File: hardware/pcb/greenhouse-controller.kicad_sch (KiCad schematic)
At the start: 47 parts, among them J1 Motor 2, J2 Screw_Terminal_01x02, J3 I2C Display, J4 Keypad, J5 MODBUS RS485, J6 Motor 3, J7 Motor 1, Q1 2N7000, Q2 2N7000, Q3 2N7000, Q4 2N7000, Q5 2N7000, Q6 2N7000, U1 Wemos_S3_ESP32-S3, U2 BUCK-30V-5V

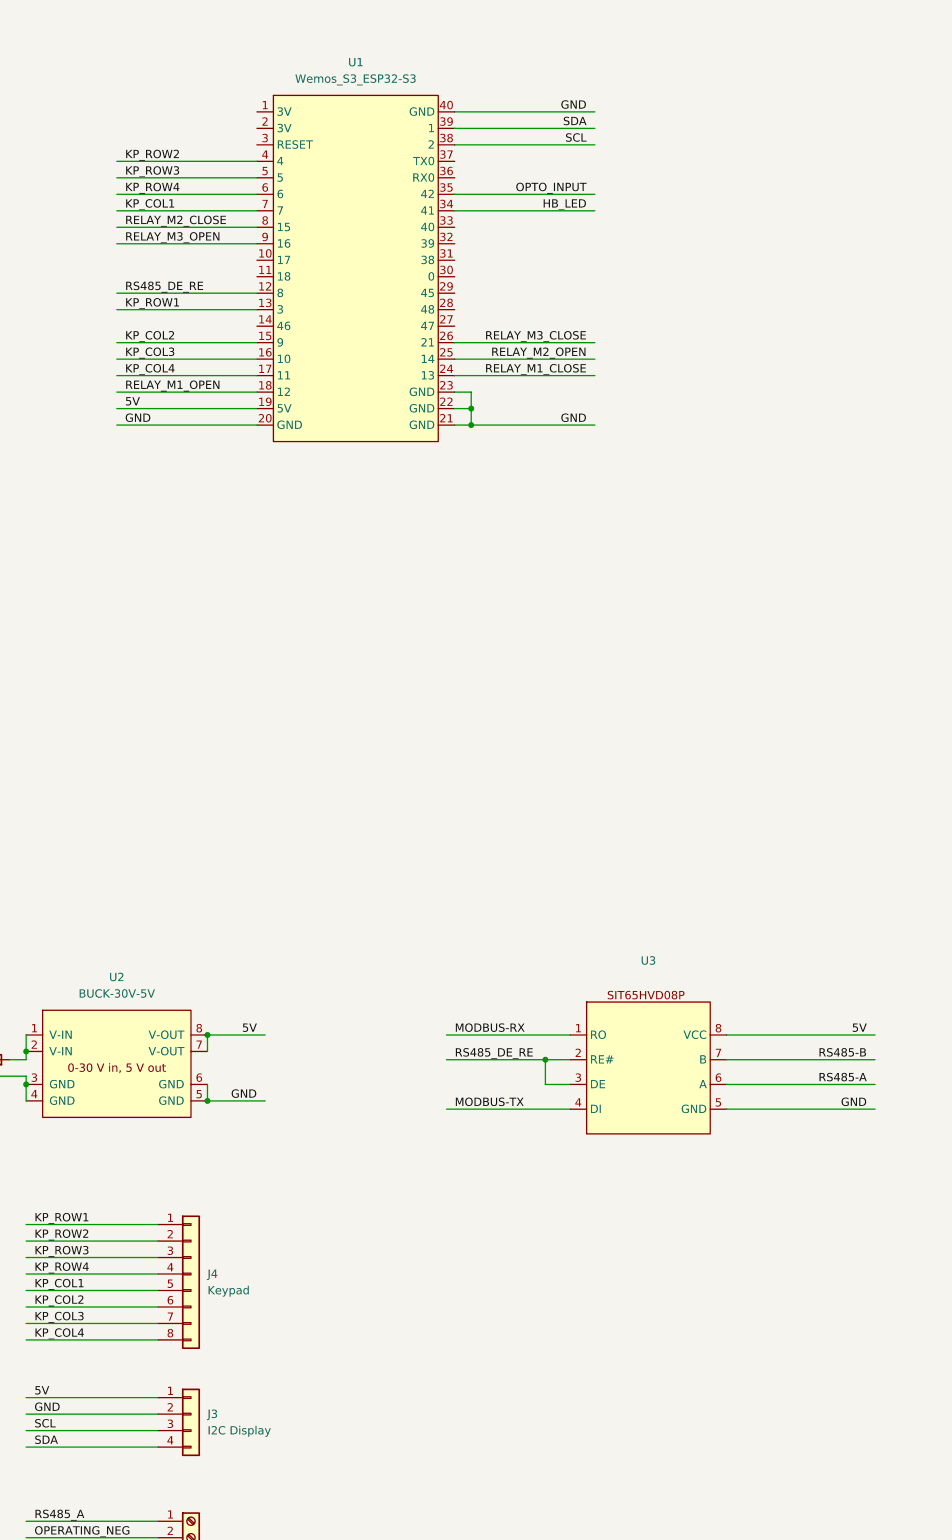
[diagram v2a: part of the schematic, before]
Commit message: Added Atomic RS485 Base documentation for development of stubs and tests. added LittleFS driver added modbus drive (not ready) added nvs driver added sdcard driver Updated PCD design
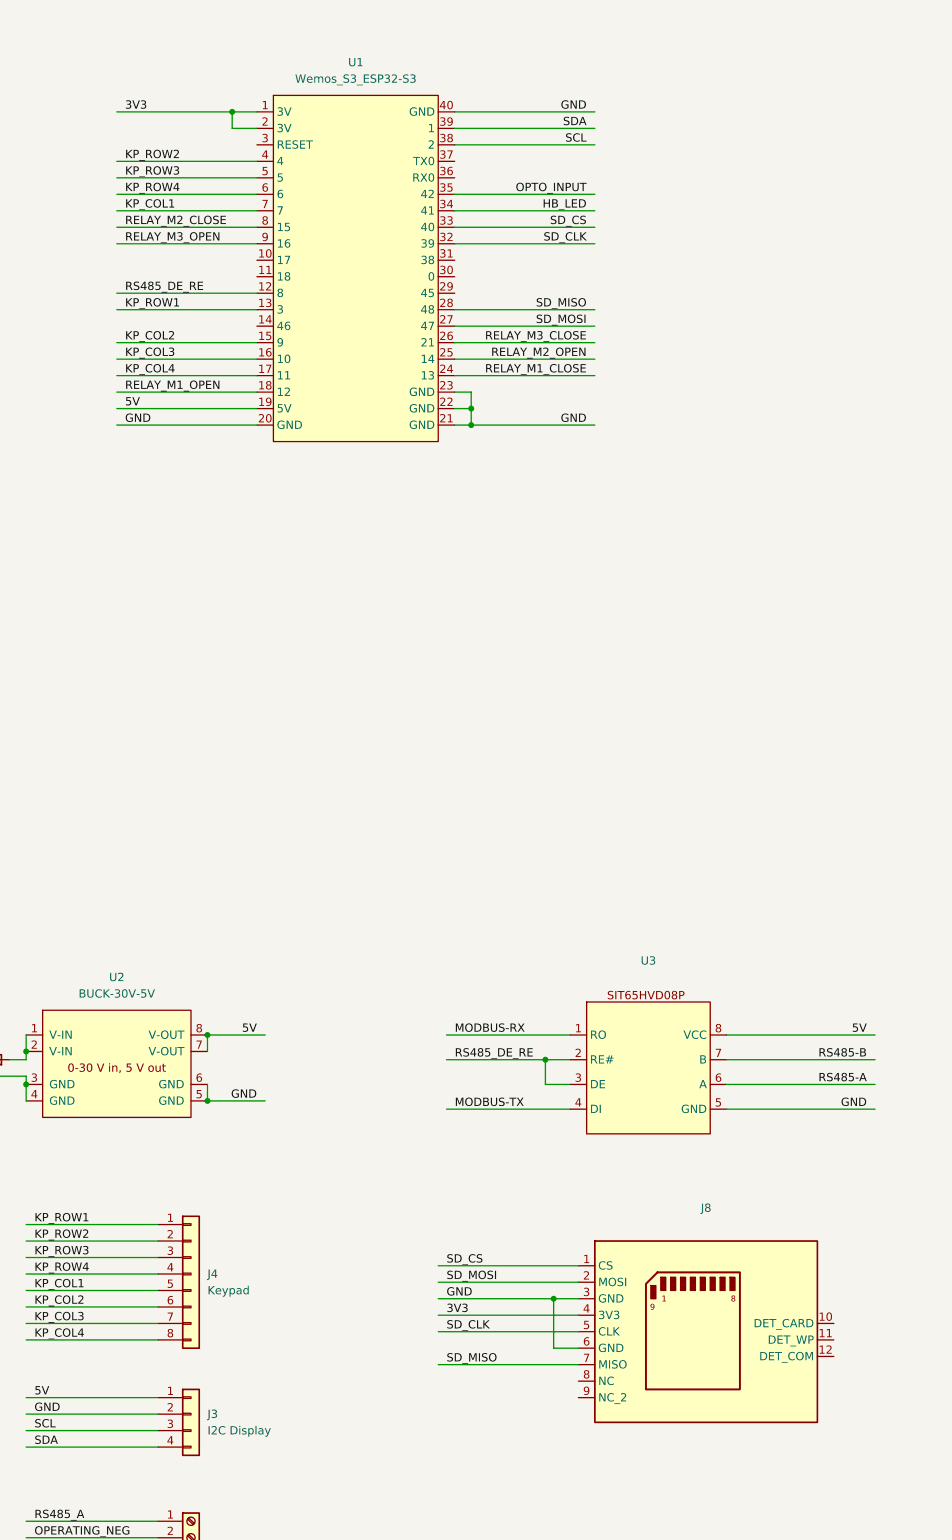
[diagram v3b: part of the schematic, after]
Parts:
- added J8: ~, symbol my-KiCad-library:SD-Socket
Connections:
- net GND: now also J8.3 (GND), J8.6 (GND)
- net 3V3: now reaches U1.1 (3V)
- net 3V3: now also U1.2 (3V), J8.4 (3V3)
- net SD_MOSI: now reaches U1.27 (47)
- net SD_MOSI: now also J8.2 (MOSI)
- net SD_MISO: now reaches U1.28 (48)
- net SD_MISO: now also J8.7 (MISO)
- net SD_CLK: now reaches U1.32 (39)
- net SD_CLK: now also J8.5 (CLK)
- net SD_CS: now reaches U1.33 (40)
- net SD_CS: now also J8.1 (CS)

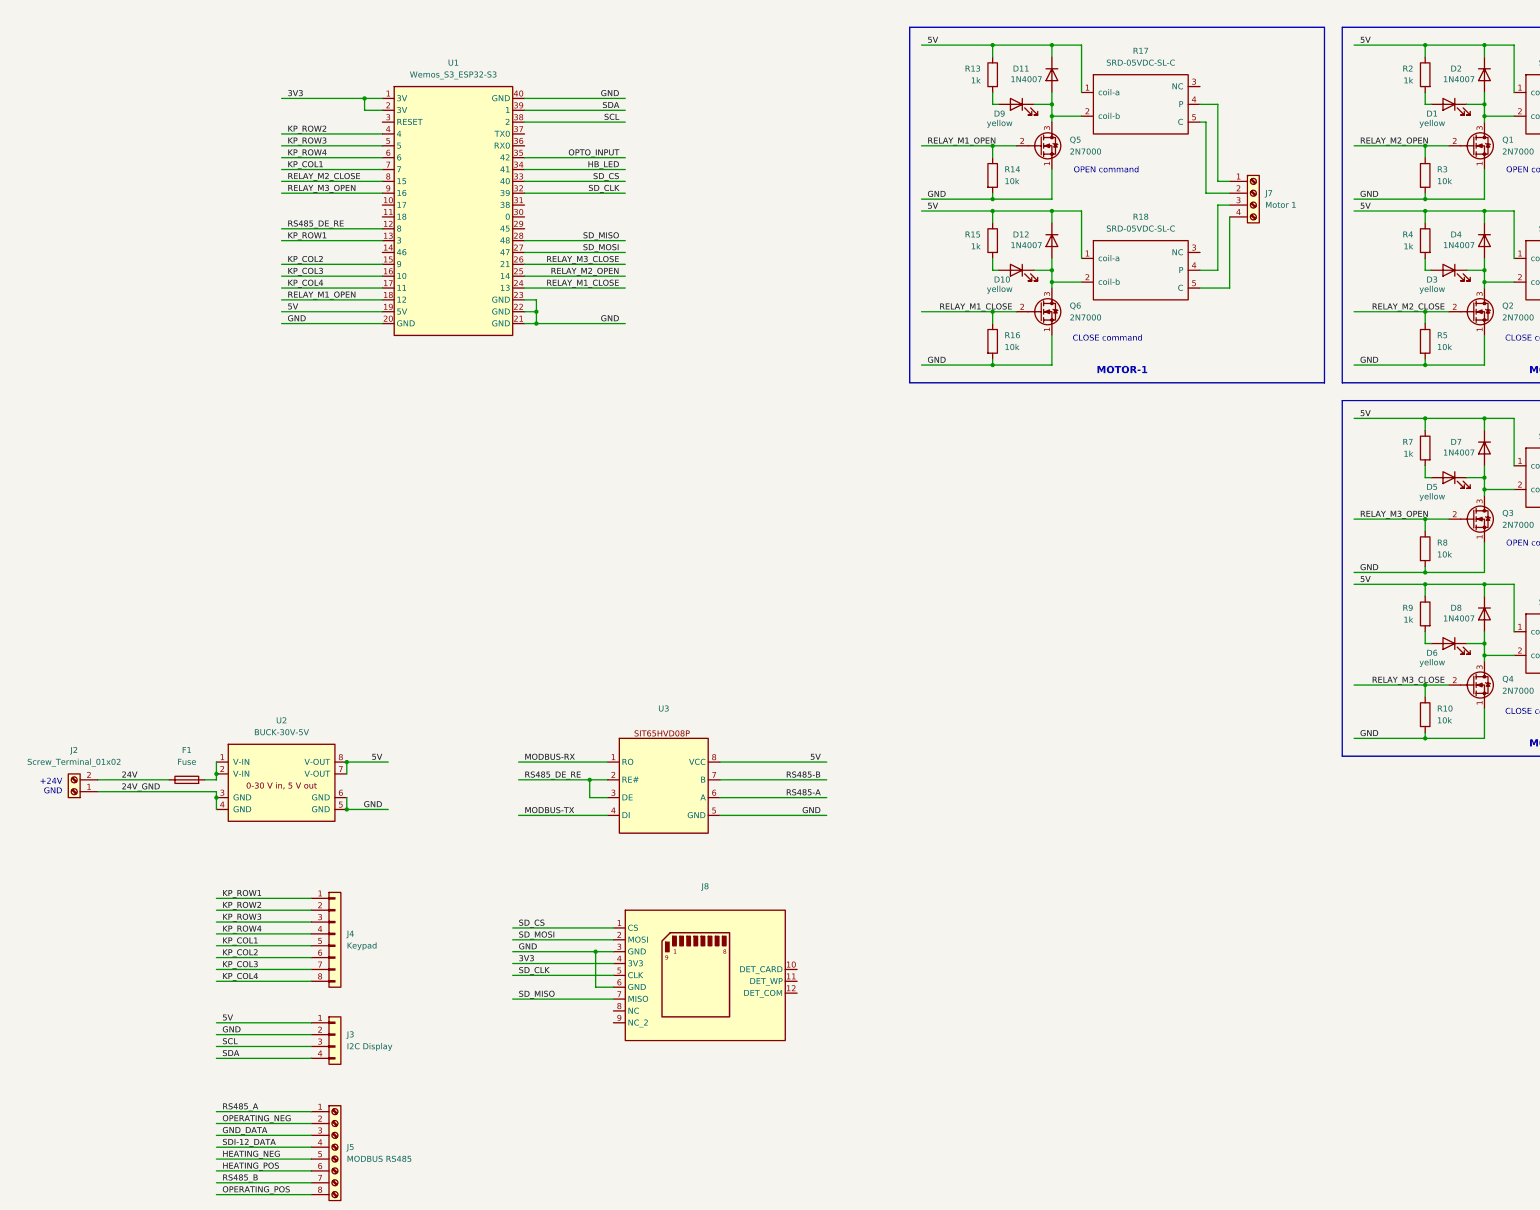
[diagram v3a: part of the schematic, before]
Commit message: updated design documentation with changes during implementation. added functional design items on led-colour use. updated schema in Kicad
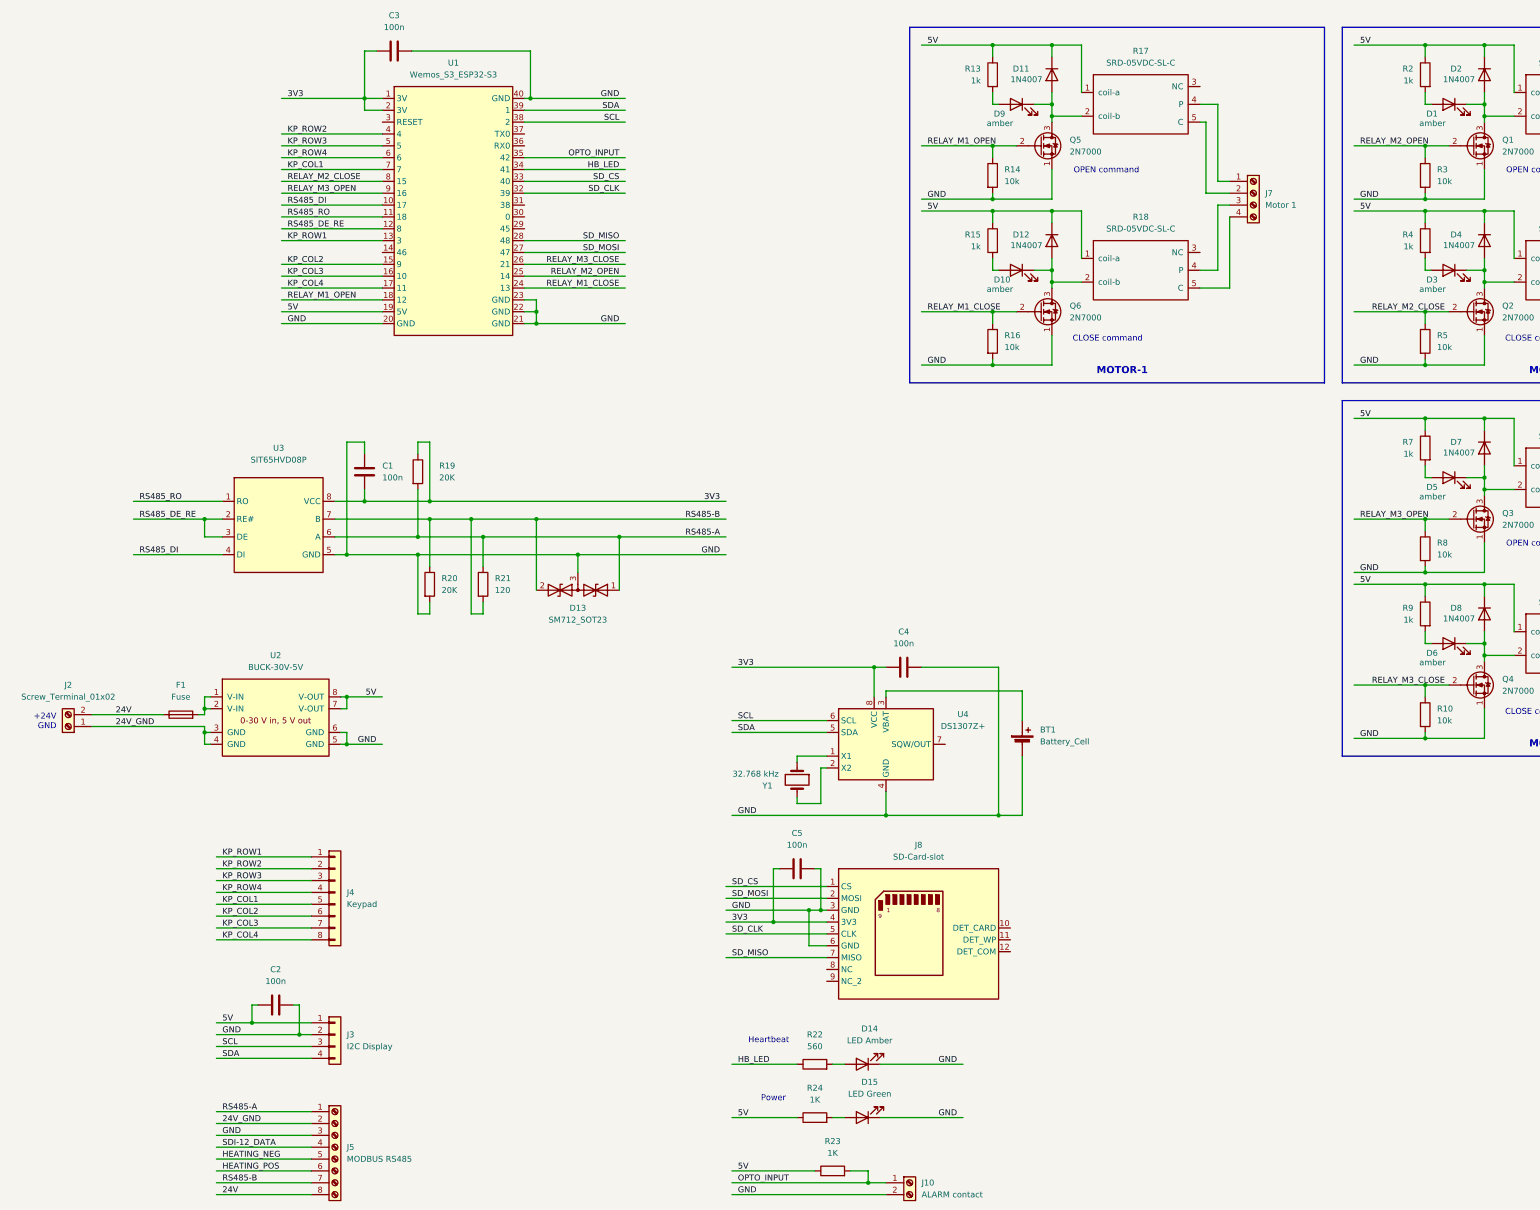
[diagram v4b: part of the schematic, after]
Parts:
- added BT1: Battery_Cell, symbol Device:Battery_Cell
- added C1, C2, C3, C4, C5: 100n, Capacitor_SMD:C_1206_3216Metric_Pad1.33x1.80mm_HandSolder, symbol Device:C
- added D13: SM712_SOT23, Package_TO_SOT_SMD:SOT-23, symbol Diode:SM712_SOT23
- added D14: LED Amber, LED_SMD:LED_0805_2012Metric_Pad1.15x1.40mm_HandSolder, symbol Device:LED
- added D15: LED Green, LED_SMD:LED_0805_2012Metric_Pad1.15x1.40mm_HandSolder, symbol Device:LED
- added J10: ALARM contact, symbol Connector:Screw_Terminal_01x02
- added R19, R20: 20K, Resistor_SMD:R_1206_3216Metric_Pad1.30x1.75mm_HandSolder, symbol Device:R
- added R21: 120, Resistor_SMD:R_1206_3216Metric_Pad1.30x1.75mm_HandSolder, symbol Device:R
- added R22: 560, Resistor_SMD:R_1206_3216Metric_Pad1.30x1.75mm_HandSolder, symbol Device:R
- added R23, R24: 1K, Resistor_SMD:R_1206_3216Metric_Pad1.30x1.75mm_HandSolder, symbol Device:R
- added U4: DS1307Z+, Package_SO:SOIC-8_3.9x4.9mm_P1.27mm, symbol Timer_RTC:DS1307Z+
- added Y1: 32.768 kHz, Crystal:Crystal_DS26_D2.0mm_L6.0mm_Horizontal_1EP_style2, symbol Device:Crystal
- D1, D10, D3, D5, D6, D9: value yellow -> amber; footprint (none) -> LED_SMD:LED_0805_2012Metric_Pad1.15x1.40mm_HandSolder
- J8: value ~ -> SD-Card-slot
- R1, R11, R12, R17, R18, R6: footprint (none) -> my-KiCad-library:SRD-05VDC-SL-C
- R10, R13, R14, R15, R16, R2, R3, R4, R5, R7, R8, R9: footprint (none) -> Resistor_SMD:R_1206_3216Metric_Pad1.30x1.75mm_HandSolder
- U1: footprint (none) -> my-KiCad-library:Wemos_S3_ESP32-S3
- U2: footprint esp32_node_footprints:BUCK-30V-5V -> my-KiCad-library:BUCK-30V-5V
- U3: value ~ -> SIT65HVD08P; footprint (none) -> Package_DIP:DIP-8_W7.62mm_LongPads
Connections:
- net GND_DATA is gone; now on net GND: J5.3 (Pin_3)
- net MODBUS-RX is gone; now on net RS485_RO: U3.1 (RO)
- net MODBUS-TX is gone; now on net RS485_DI: U3.4 (DI)
- net OPERATING_NEG is gone; now on net 24V_GND: J5.2 (Pin_2)
- net OPERATING_POS is gone; now on net 24V: J5.8 (Pin_8)
- net RS485_A is gone; now on net RS485-A: J5.1 (Pin_1)
- net RS485_B is gone; now on net RS485-B: J5.7 (Pin_7)
- net 3V3: now also U3.8 (VCC), C1.2, C3.1, C4.1, C5.1, R19.1, U4.8 (VCC)
- net 5V: now also C2.1, R23.1, R24.1; no longer U3.8 (VCC)
- net GND: now also BT1.2 (-), C1.1, C2.2, C3.2, C4.2, C5.2, D13.3 (common), D14.1 (K), D15.1 (K), J10.2 (Pin_2), R20.2, U4.4 (GND)
- net HB_LED: now also R22.1
- net OPTO_INPUT: now also J10.1 (Pin_1), R23.2
- net RS485-A: now also D13.1 (A1), R19.2, R21.1
- net RS485-B: now also D13.2 (A2), R20.1, R21.2
- net SCL: now also U4.6 (SCL)
- net SDA: now also U4.5 (SDA)
- net RS485_DI: now reaches U1.10 (17)
- net RS485_RO: now reaches U1.11 (18)
- net RELAY_M1_OPEN: now reaches Q5.2 (G), R14.1, U1.18 (12)
- new net: D14.2 (A), R22.2
- new net: BT1.1 (+), U4.3 (VBAT)
- new net: U4.1 (X1), Y1.1
- new net: U4.2 (X2), Y1.2
- new net: D15.2 (A), R24.2
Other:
- note added: "Heartbeat"
- note added: "Power"
- moved on the sheet: F1, J2, J4, J8, U2
